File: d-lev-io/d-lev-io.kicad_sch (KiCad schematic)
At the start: 9 parts, among them J1 PJ-059A, J2 USB_C_Receptacle_USB2.0, U1 AMS1117-5.0

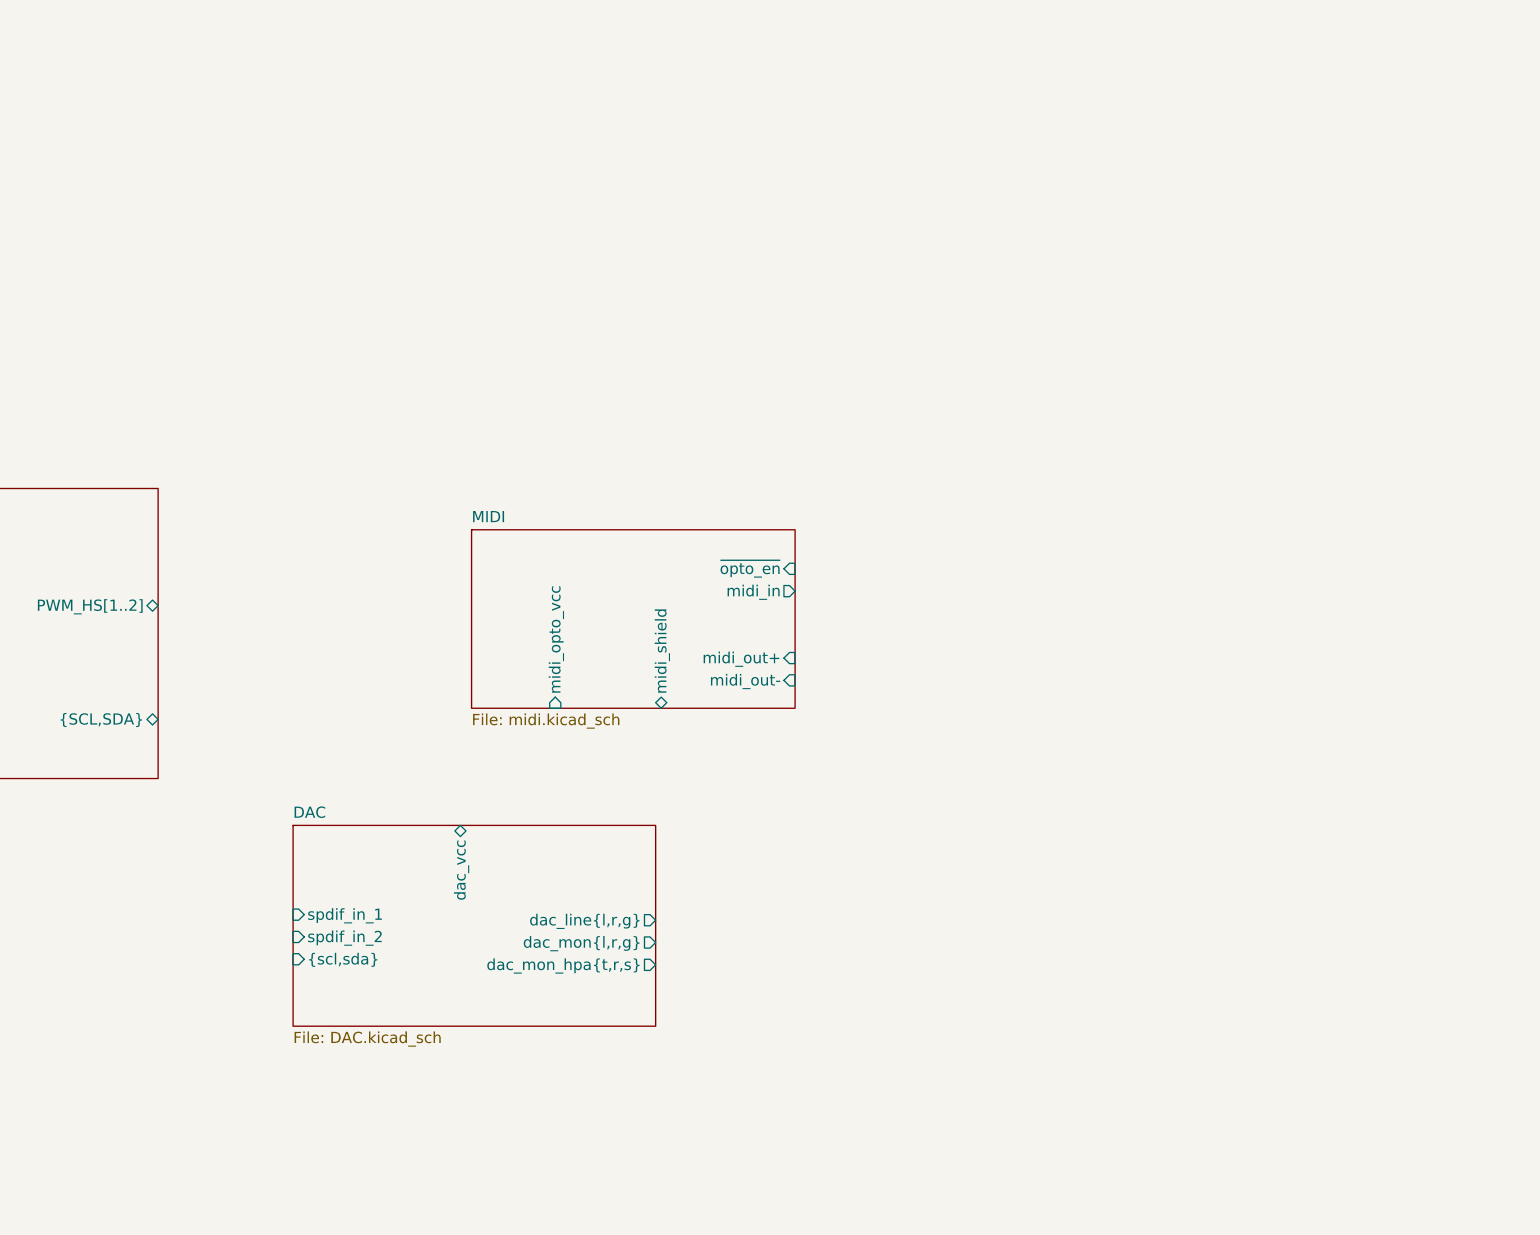
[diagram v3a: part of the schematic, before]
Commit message: clean up 3d models
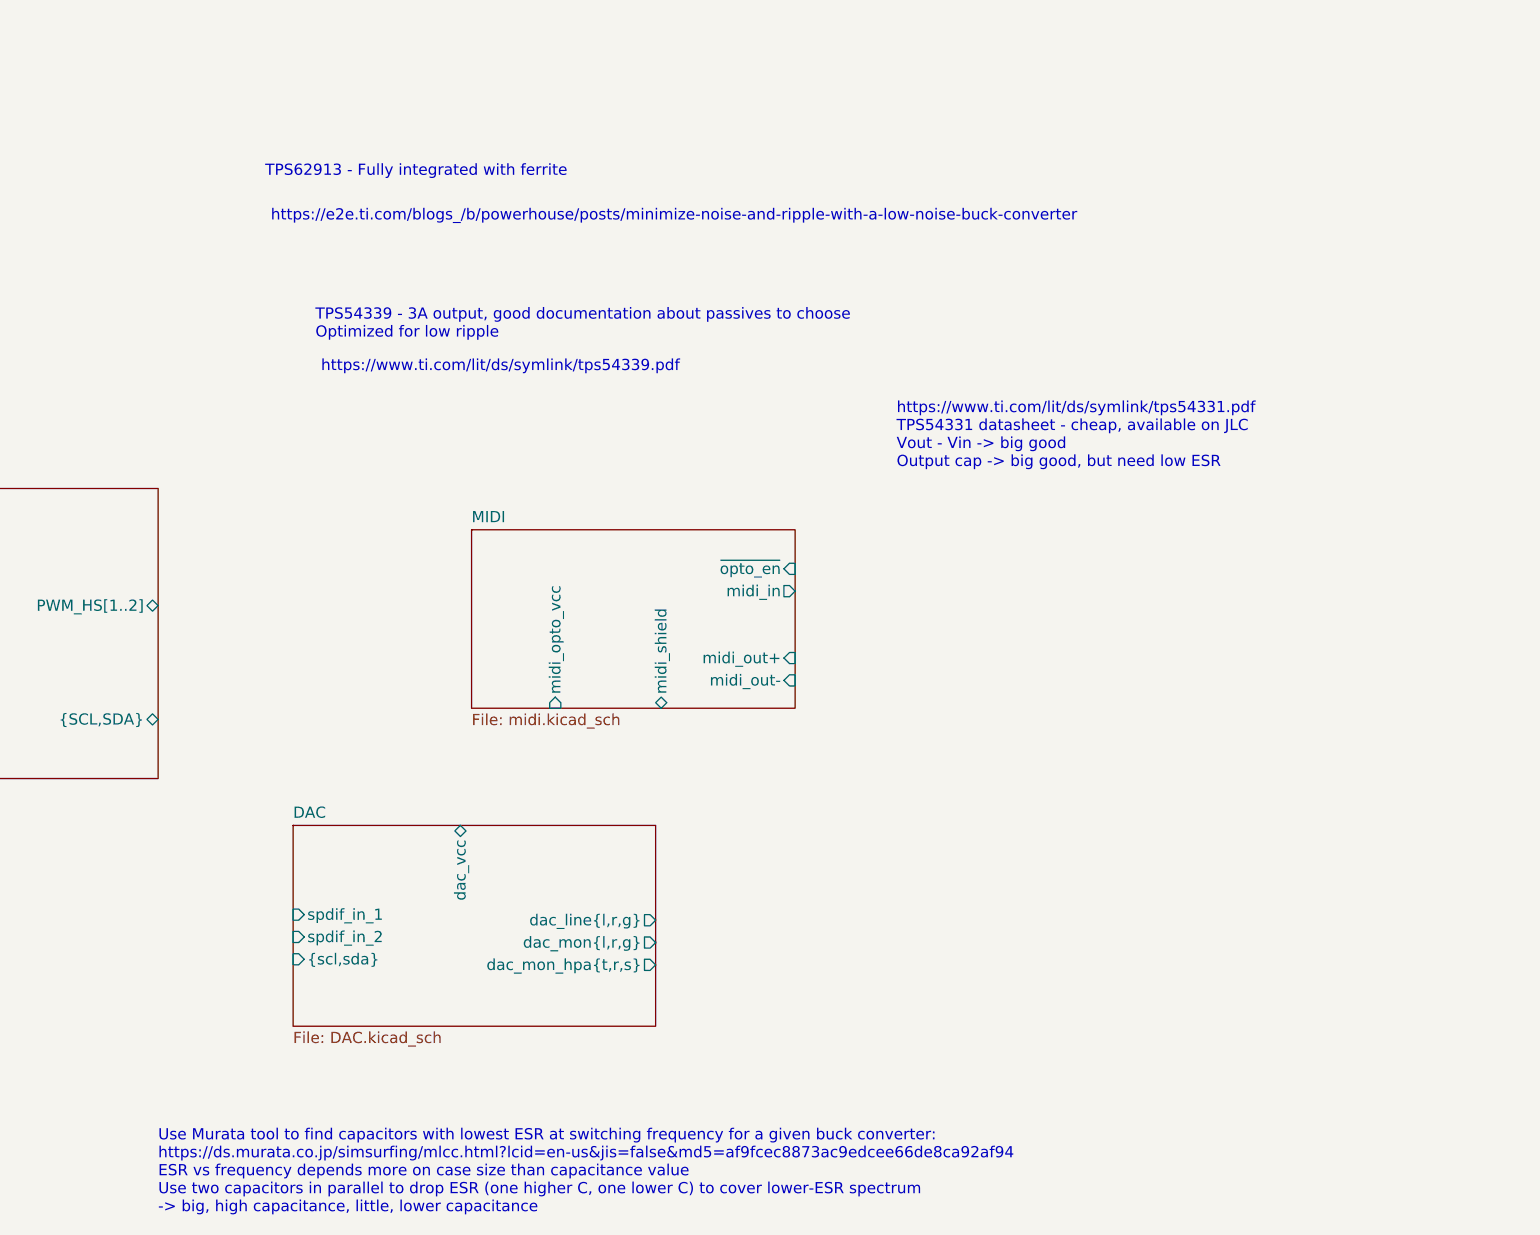
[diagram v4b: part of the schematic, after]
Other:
- note added: "TPS54339 - 3A output, good documentation about passives to choose Optimized for low ripple"
- note added: "TPS62913 - Fully integrated with ferrite"
- note added: "Use Murata tool to find capacitors with lowest ESR at switching frequency for a given buck converter: https://ds.murata.co.jp/simsurfing/mlcc.html?lcid=en-us&jis=false&md5=af9fcec8873ac9edcee66de8ca92af94 ESR vs frequency depends more on case size than capacitance value Use two capacitors in parallel to drop ESR (one higher C, one lower C) to cover lower-ESR spectrum -> big, high capacitance, lit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"
- note added: "https://e2e.ti.com/blogs_/b/powerhouse/posts/minimize-noise-and-ripple-with-a-low-noise-buck-converter"
- note added: "https://www.ti.com/lit/ds/symlink/tps54331.pdf TPS54331 datasheet - cheap, available on JLC Vout - Vin -> big good Output cap -> big good, but need low ESR"
- note added: "https://www.ti.com/lit/ds/symlink/tps54339.pdf"
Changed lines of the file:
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@@
     (effects (font (size 2 2)) (justify left top))
+  )
+  (text "https://e2e.ti.com/blogs_/b/powerhouse/posts/minimize-noise-and-ripple-with-a-low-noise-buck-converter"
+    (at 161.925 29.845 0)
+    (effects (font (size 1.27 1.27)) (justify left bottom))
+  )
+  (text "Use Murata tool to find capacitors with lowest ESR at switching frequency for a given buck converter:\nhttps://ds.murata.co.jp/simsurfing/mlcc.html?lcid=en-us&jis=false&md5=af9fcec8873ac9edcee66de8ca92af94\nESR vs frequency depends more on case size than capacitance value\nUse two capacitors in parallel to drop ESR (one higher C, one lower C) to cover lower-ESR spectrum\n-> big, high capacitance, little, lower capacitance"
+    (at 149.098 142.748 0)
+    (effects (font (size 1.27 1.27)) (justify left bottom))
+  )
+  (text "https://www.ti.com/lit/ds/symlink/tps54339.pdf" (at 167.64 46.99 0)
+    (effects (font (size 1.27 1.27)) (justify left bottom))
+  )
+  (text "TPS54339 - 3A output, good documentation about passives to choose\nOptimized for low ripple"
+    (at 167.005 43.18 0)
+    (effects (font (size 1.27 1.27)) (justify left bottom))
   )
   (text "SPDIF (Line)" (at 191.135 -46.4312 90)
@@
   (text "Recommend use with power brick: Meanwell SGAS15A12-P1J"
     (at 16.51 18.415 0)
+    (effects (font (size 1.27 1.27)) (justify left bottom))
+  )
+  (text "https://www.ti.com/lit/ds/symlink/tps54331.pdf\nTPS54331 datasheet - cheap, available on JLC\nVout - Vin -> big good\nOutput cap -> big good, but need low ESR\n"
+    (at 233.172 57.912 0)
     (effects (font (size 1.27 1.27)) (justify left bottom))
   )
@@
     (effects (font (size 1.27 1.27)) (justify left bottom))
   )
+  (text "TPS62913 - Fully integrated with ferrite" (at 161.29 24.765 0)
+    (effects (font (size 1.27 1.27)) (justify left bottom))
+  )
   (text "GND" (at 102.235 -45.72 90)
     (effects (font (size 1.27 1.27)) (justify left bottom))
@@
     (effects (font (size 1.27 1.27)) (justify left bottom))
   )
-  (label "USB.DM" (at 66.04 69.85 0)
+  (label "USB.DM" (at 66.04 69.85 0) (fields_autoplaced)
     (effects (font (size 1.27 1.27)) (justify left bottom))
   )
@@
     (effects (font (size 1.27 1.27)) (justify right bottom))
   )
-  (label "USB.DP" (at 66.04 74.93 0)
+  (label "USB.DP" (at 66.04 74.93 0) (fields_autoplaced)
     (effects (font (size 1.27 1.27)) (justify left bottom))
   )

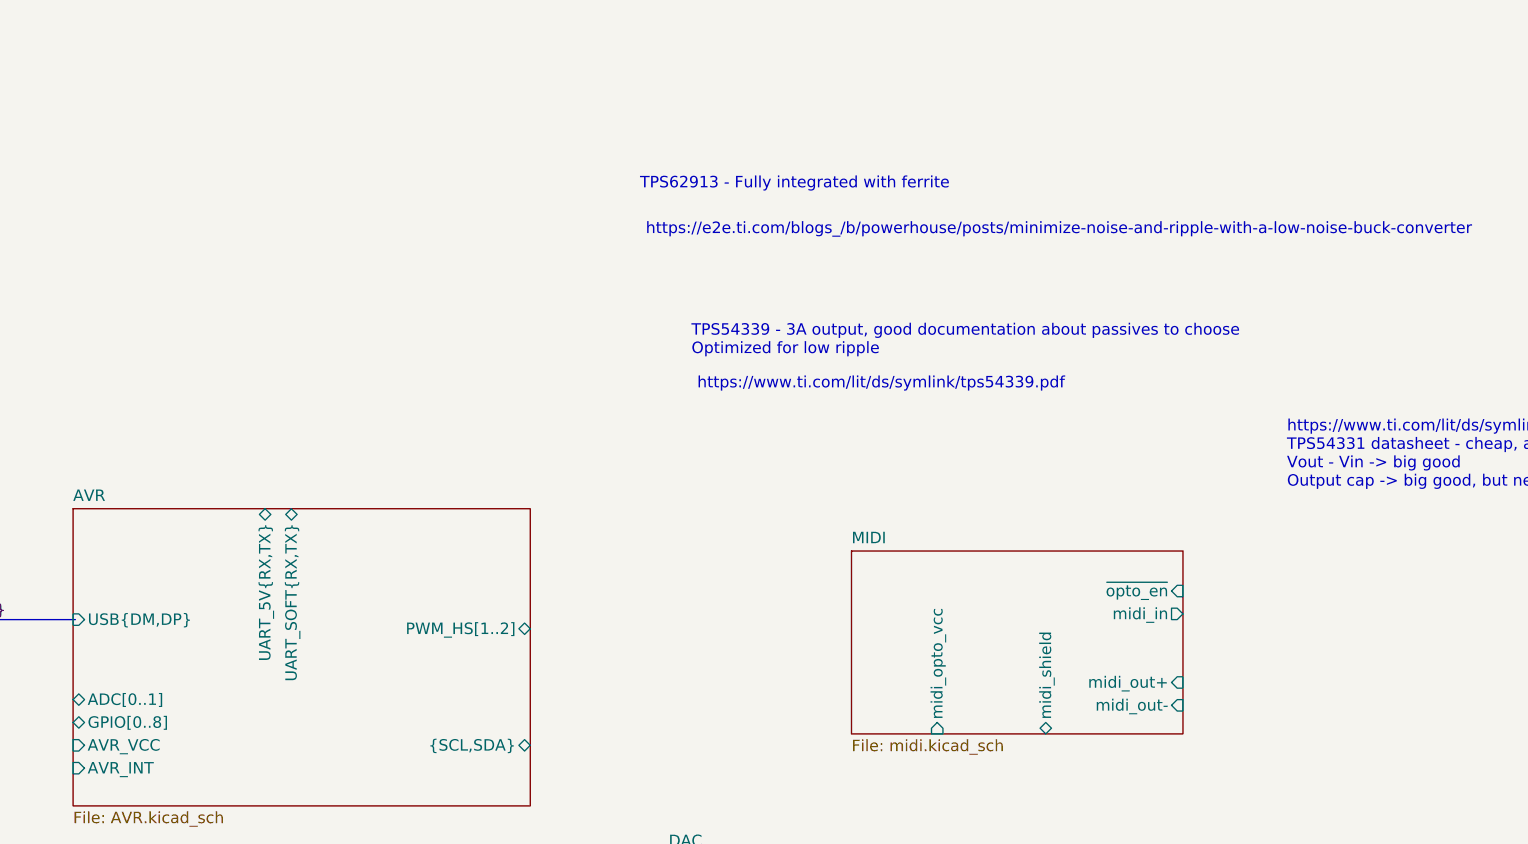
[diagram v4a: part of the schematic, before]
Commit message: Level shifters and rearrange encoders
* WIP: use net buses more effectively to organize encoder signals
* Add application note for level shifters
* Add level shifters for UART, change MIDI level shifter BJT to FET
* Add MIDI_HI pull-up on d-lev-io board
* Add/change some footprints
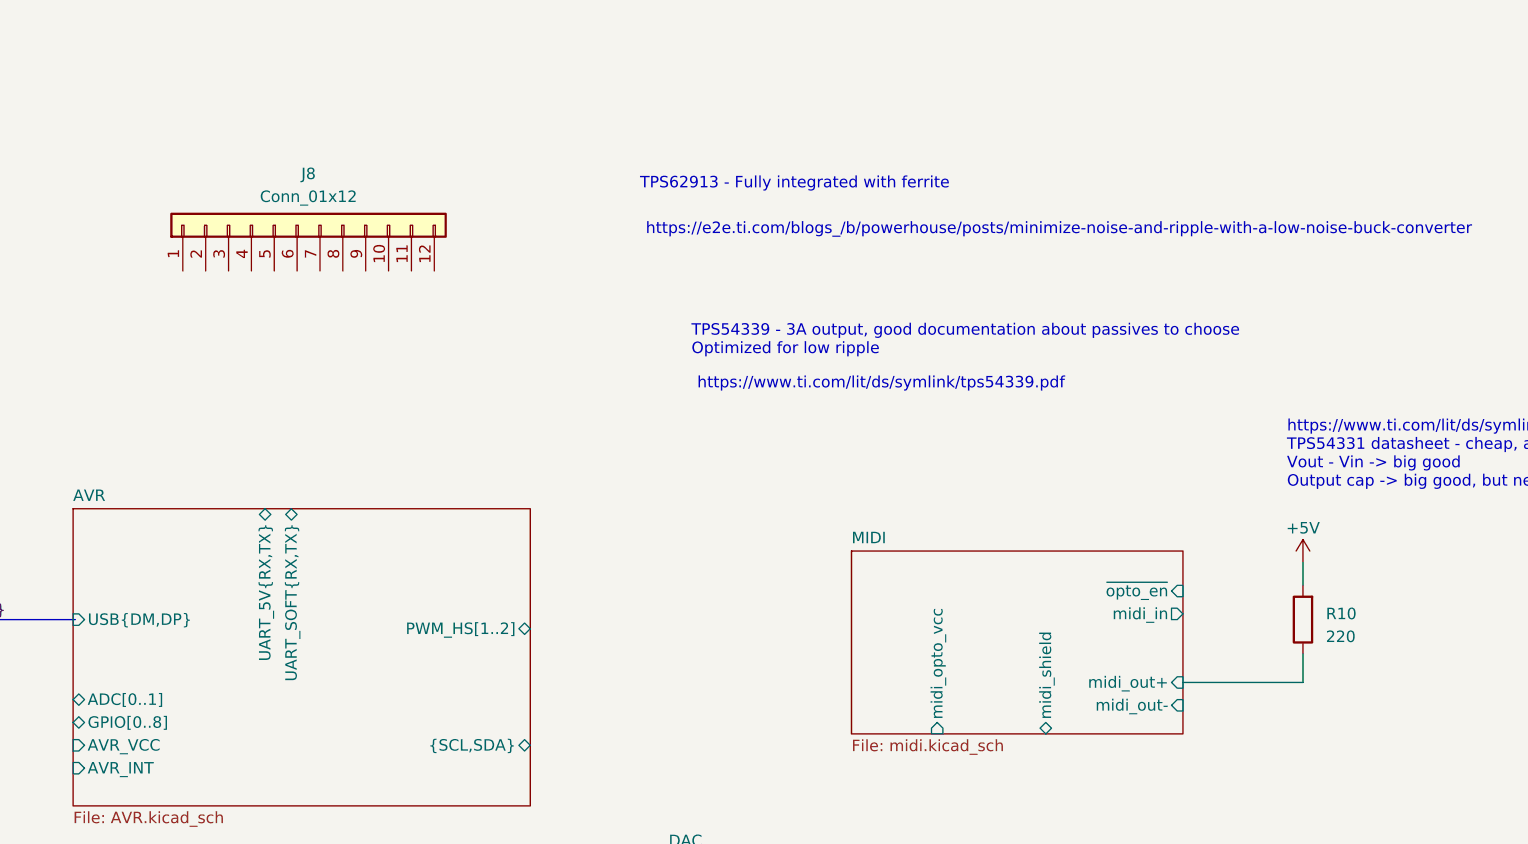
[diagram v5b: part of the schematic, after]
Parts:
- added J8: Conn_01x12, Connector_JST:JST_PH_S12B-PH-SM4-TB_1x12-1MP_P2.00mm_Horizontal, symbol Connector_Generic:Conn_01x12
- added R10: 220, symbol Device:R
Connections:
- net MIDI/midi_out+: now also R10.1
- new net +5V: R10.2
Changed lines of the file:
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@@
+    (stroke (width 0) (type default))
+  )
+  (wire (pts (xy 234.95 76.2) (xy 234.95 79.375))
     (stroke (width 0) (type default))
   )
@@
   )
   (wire (pts (xy 57.15 63.5) (xy 57.15 64.77))
+    (stroke (width 0) (type default))
+  )
+  (wire (pts (xy 234.95 66.04) (xy 234.95 68.58))
+    (stroke (width 0) (type default))
+  )
+  (wire (pts (xy 234.95 79.375) (xy 221.615 79.375))
     (stroke (width 0) (type default))
   )
@@
     )
   )
+  (symbol (lib_id "power:+5V") (at 234.95 66.04 0) (unit 1)
+    (in_bom yes) (on_board yes) (dnp no) (fields_autoplaced)
+    (property "Reference" "#PWR018" (at 234.95 69.85 0)
+      (effects (font (size 1.27 1.27)) hide)
+    )
+    (property "Value" "+5V" (at 234.95 62.23 0)
+      (effects (font (size 1.27 1.27)))
+    )
+    (property "Footprint" "" (at 234.95 66.04 0)
+      (effects (font (size 1.27 1.27)) hide)
+    )
+    (property "Datasheet" "" (at 234.95 66.04 0)
+      (effects (font (size 1.27 1.27)) hide)
+    )
+    (pin "1")
+    (instances
+      (project "d-lev-io"
+        (path "/9261a07b-ae4a-4d72-8042-ea097cd0e5ed"
+          (reference "#PWR018") (unit 1)
+        )
+      )
+    )
+  )
+  (symbol (lib_id "Connector_Generic:Conn_01x12") (at 123.19 28.575 90) (unit 1)
+    (in_bom yes) (on_board yes) (dnp no)
+    (property "Reference" "J8" (at 124.46 22.86 90)
+      (effects (font (size 1.27 1.27)))
+    )
+    (property "Value" "Conn_01x12" (at 124.46 25.4 90)
+      (effects (font (size 1.27 1.27)))
+    )
+    (property "Footprint" "Connector_JST:JST_PH_S12B-PH-SM4-TB_1x12-1MP_P2.00mm_Horizontal" (at 123.19 28.575 90)
+      (effects (font (size 1.27 1.27)) hide)
+    )
+    (property "Datasheet" "~" (at 123.19 28.575 0)
+      (effects (font (size 1.27 1.27)) hide)
+    )
+    (pin "1")
+    (pin "10")
+    (pin "11")
+    (pin "12")
+    (pin "2")
+    (pin "3")
+    (pin "4")
+    (pin "5")
+    (pin "6")
+    (pin "7")
+    (pin "8")
+    (pin "9")
+    (instances
+      (project "d-lev-io"
+        (path "/9261a07b-ae4a-4d72-8042-ea097cd0e5ed"
+          (reference "J8") (unit 1)
+        )
+      )
+    )
+  )
   (symbol (lib_id "Device:R_Small") (at 54.61 73.66 270) (unit 1)
     (in_bom yes) (on_board yes) (dnp no)
@@
         )
       )
+    )
+  )
+  (symbol (lib_id "Device:R") (at 234.95 72.39 180) (unit 1)
+    (in_bom yes) (on_board yes) (dnp no) (fields_autoplaced)
+    (property "Reference" "R10" (at 237.49 71.755 0)
+      (effects (font (size 1.27 1.27)) (justify right))
+    )
+    (property "Value" "220" (at 237.49 74.295 0)
+      (effects (font (size 1.27 1.27)) (justify right))
+    )
+    (property "Footprint" "" (at 236.728 72.39 90)
+      (effects (font (size 1.27 1.27)) hide)
+    )
+    (property "Datasheet" "~" (at 234.95 72.39 0)
+      (effects (font (size 1.27 1.27)) hide)
+    )
+    (pin "1")
+    (pin "2")
+    (instances
+      (project "d-lev-io"
+        (path "/9261a07b-ae4a-4d72-8042-ea097cd0e5ed"
+          (reference "R10") (unit 1)
+        )
+      )

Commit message: more minor pusharounds and updates
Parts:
- removed J8: Conn_01x12, Connector_JST:JST_PH_S12B-PH-SM4-TB_1x12-1MP_P2.00mm_Horizontal, symbol Connector_Generic:Conn_01x12
- added J8: Conn_01x12_MountingPin, theremin:JST_PH_S12B-PH-SM4-TB_1x12-1MP_P2.00mm_Horizontal, symbol Connector_Generic_MountingPin:Conn_01x12_MountingPin
- J1: footprint (none) -> theremin:BarrelJack_CUI_PJ-059A
- R10: footprint (none) -> Resistor_SMD:R_0603_1608Metric
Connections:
- net +5V: now also J8.12 (Pin_12)
- net GND: now also J8.1 (Pin_1), J8.11 (Pin_11)
- new net acal_btn: J8.4 (Pin_4)
- new net midi_from_fpga: J8.8 (Pin_8)
- new net midi_to_fpga: J8.7 (Pin_7)
- new net mute_btn: J8.3 (Pin_3)
- new net mute_led: J8.2 (Pin_2)
- new net spdif_line: J8.6 (Pin_6)
- new net spdif_mon: J8.5 (Pin_5)
- new net uart_rx_5v: J8.10 (Pin_10)
- new net uart_tx_5v: J8.9 (Pin_9)
- no-connect marks 0 -> 1
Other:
- note added: "midi_out: 5V logic from D-Lev to 3-pin connector and to UART_SOFT_RX"
- moved on the sheet: U1
